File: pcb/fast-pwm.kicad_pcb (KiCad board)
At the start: 2 copper layers, 64 x 45 mm, 44 parts, among them J2 Клемма питания, J3 Выходная клемма, Q1 2N3904, Q10 AOD4184A, Q11 AOD4184A, Q12 AOD4184A, Q2 2N3905, Q3 2N3904, Q4 2N3905, Q5 2N3904, Q6 2N3905, Q7 2N3904, Q8 2N3905, Q9 AOD4184A, U1 STM32F030K6Tx, U2 MC33063AD

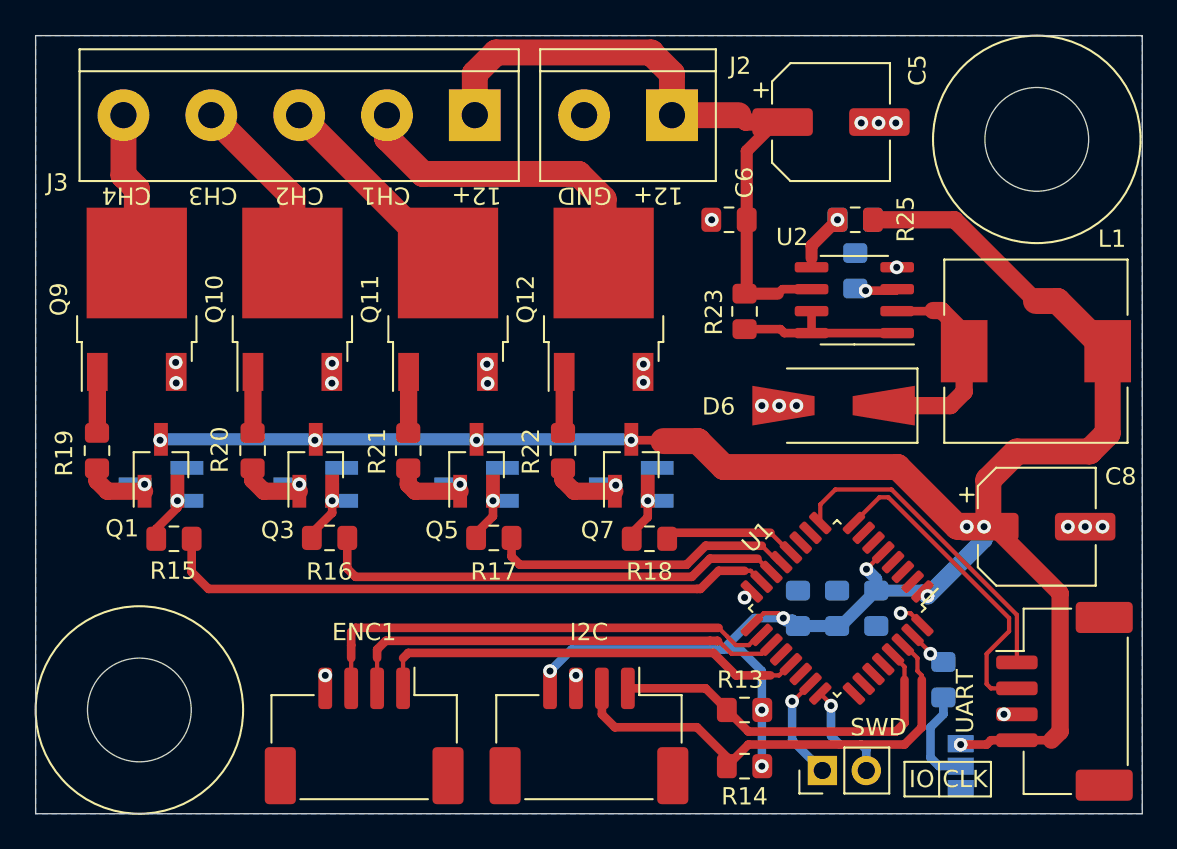
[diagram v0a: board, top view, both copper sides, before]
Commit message: исправление ошибки на шелке
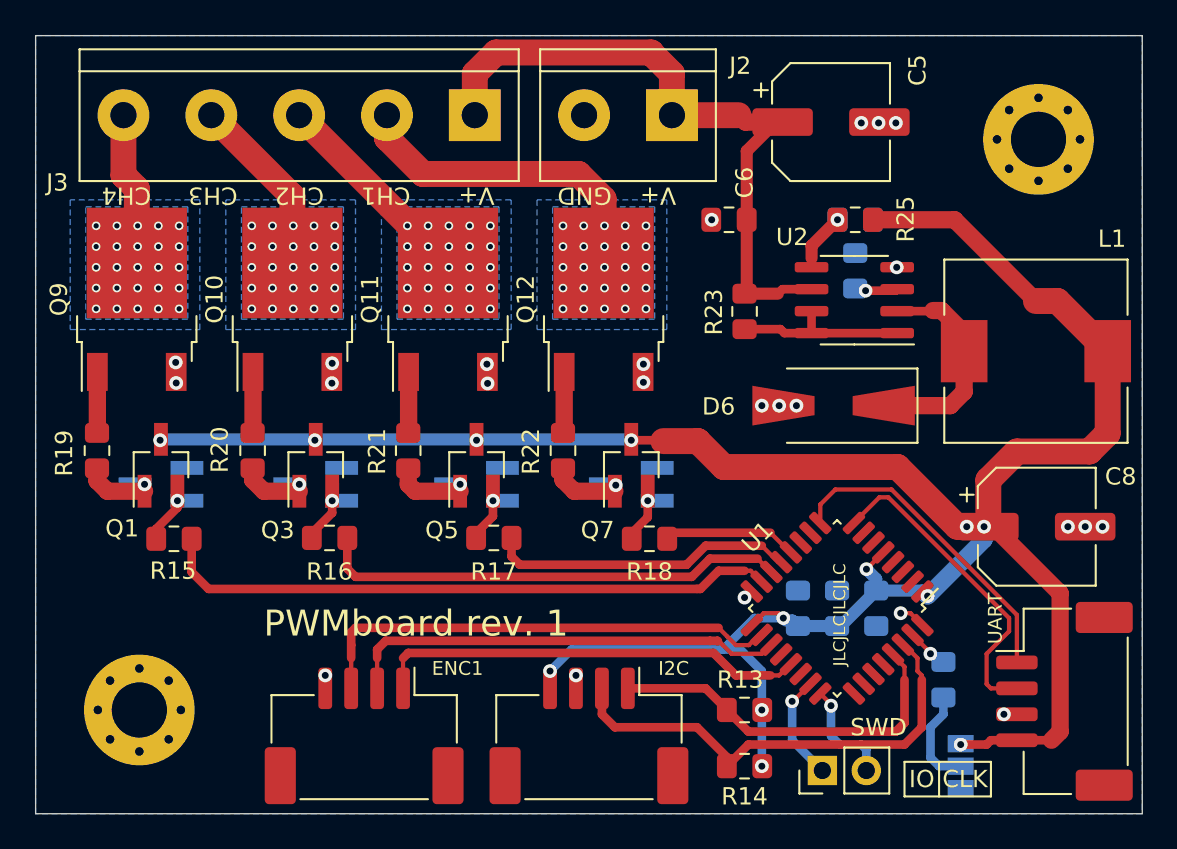
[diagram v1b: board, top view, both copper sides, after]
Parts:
- added REF**: MountingHole_3.2mm_M3_Pad_Via, MountingHole:MountingHole_3.2mm_M3_Pad_Via, F.Cu at (33.0, 156.0)
- added REF**: MountingHole_3.2mm_M3_Pad_Via, MountingHole:MountingHole_3.2mm_M3_Pad_Via, F.Cu at (85.0, 123.0)
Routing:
- net CH4: vias 0 -> 25
- net CH3: vias 0 -> 25
- net CH2: vias 0 -> 25
- net CH1: vias 0 -> 25
- added copper zone on B.Cu, net CH1
- added copper zone on B.Cu, net CH2
- added copper zone on B.Cu, net CH3
- added copper zone on B.Cu, net CH4
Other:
- outline, holes or cut-outs redrawn
- board text added: "JLCJLCJLCJLC"
- board text added: "PWMboard rev. 1"
- board text added: "V+"
- board text removed: "12+"

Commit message: изменил номер ревизии
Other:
- board text added: "PWMboard rev. 2"
- board text removed: "PWMboard rev. 1"
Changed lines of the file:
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@@
   (page A4)
   (layers
-    (0 F.Cu signal hide)
+    (0 F.Cu signal)
     (31 B.Cu signal hide)
     (32 B.Adhes user hide)
@@
     (effects (font (size 0.7 0.7) (thickness 0.15)))
   )
-  (gr_text "PWMboard rev. 1" (at 49 151) (layer F.SilkS)
+  (gr_text "PWMboard rev. 2" (at 49 151) (layer F.SilkS)
     (effects (font (size 1.5 1.5) (thickness 0.15)))
   )
